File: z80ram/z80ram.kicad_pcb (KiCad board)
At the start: 2 copper layers, 99.8 x 49.9 mm, 19 parts, among them J1 BUS, J2 BUSEXT, Q1 2N7000, U1 Z80CPU, U2 74HCT574, U3 74LS257, U4 AS6C4008-55PCN, U5 74LS138, U6 DS1302+, Y1 XTAL

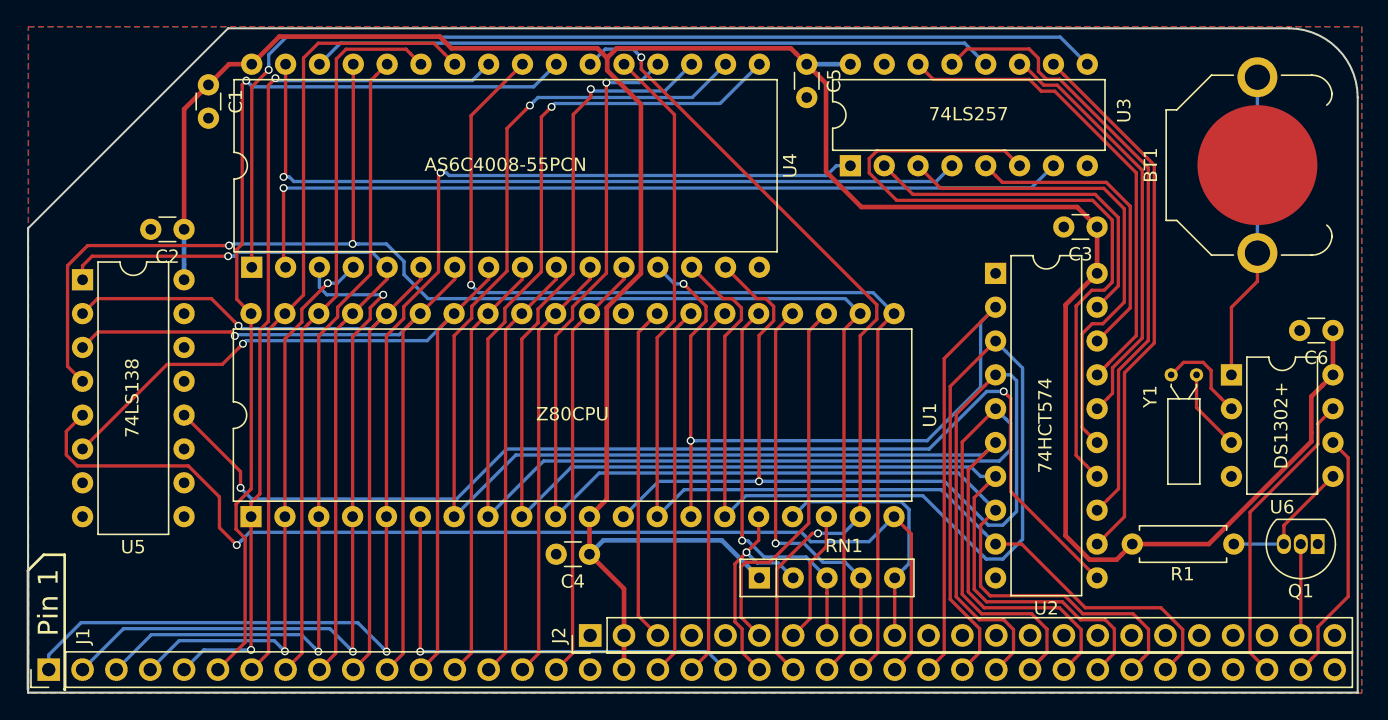
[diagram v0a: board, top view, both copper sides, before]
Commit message: Fix address decoding, minor REV2 tweaks
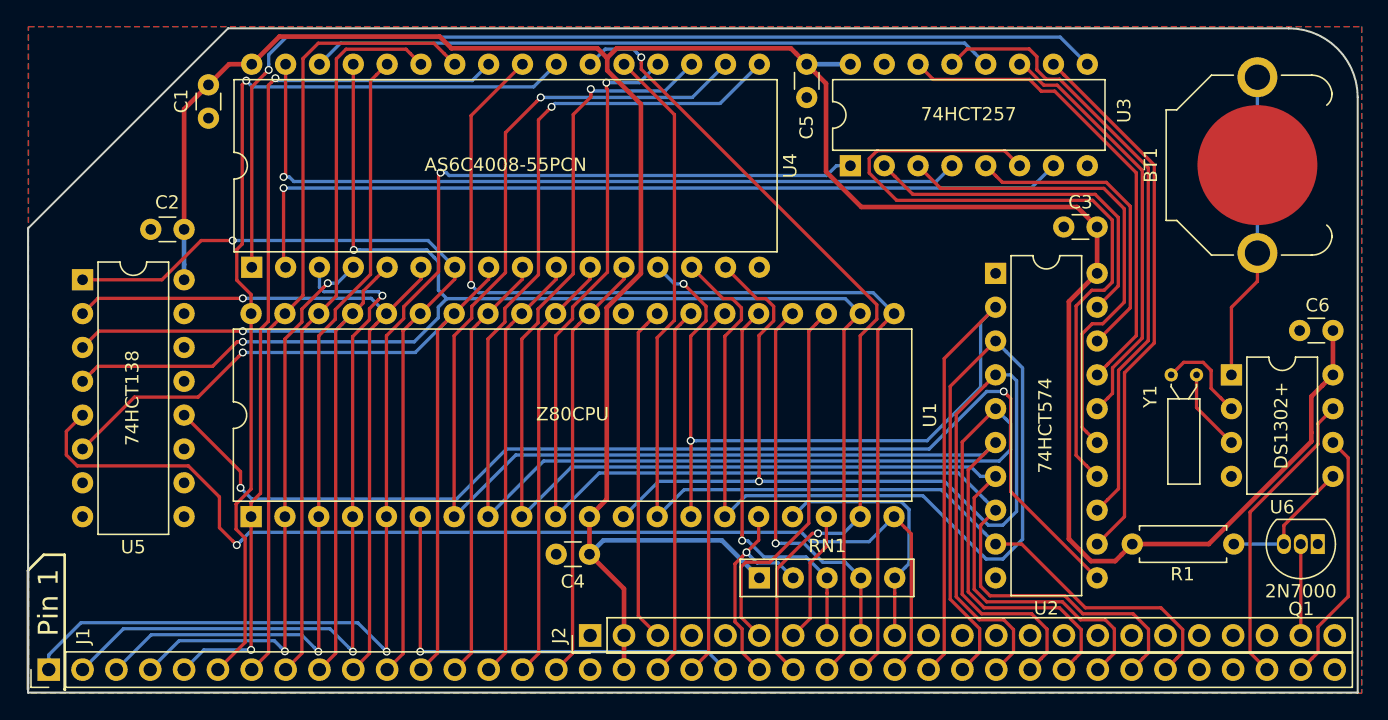
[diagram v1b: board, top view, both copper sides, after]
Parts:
- C1, C2, C3, C4, C5, C6: value C -> 0.1uf
- R1: value R -> 1M
- U3: value 74LS257 -> 74HCT257
- U5: value 74LS138 -> 74HCT138
- Y1: value XTAL -> 32.768kHz
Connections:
- U5 pad 1: /A7 -> /A5
- U5 pad 3: /A5 -> /A7
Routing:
- net /A7: track 57.1 -> 53.6 mm
- net /A5: track 59.0 -> 62.3 mm
- net /A6: track 57.0 -> 56.1 mm
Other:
- board text added: "z80ctrl CPU/RAM/RTC Board REV2 (C)2020 J.B. Langston https://github.com/jblang/z80ctrl"
- board text removed: "z80ctrl CPU/RAM/RTC Board REV1 (C)2020 J.B. Langston https://github.com/jblang/z80ctrl"

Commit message: Fix VCC1/VCC2 mixup on RTC, better layout for RTC crystal
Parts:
- R1: value 1M -> 10K
- moved C6 17.5 mm to (237.9, 136.3), turned to 90 degrees
- moved R1 16.7 mm to (240.8, 126.0)
- moved Y1 9.59 mm to (243.7, 138.3)
- moved U6 7.73 mm to (240.9, 136.3), turned to 90 degrees
- moved Q1 3.44 mm to (248.4, 144.5), turned to 0 degrees
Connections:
- U6 pad 1: Net-(BT1-Pad1) -> VCC
- U6 pad 8: VCC -> Net-(BT1-Pad1)
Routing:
- net Net-(Q1-Pad3): track 10.4 -> 19.6 mm
- net /MISO: track 19.0 -> 26.9 mm
- net VCC: track 217.2 -> 211.7 mm
- net /SCK: track 22.7 -> 27.9 mm
- net Net-(U6-Pad2): track 7.14 -> 2.13 mm
- net Net-(U6-Pad3): track 6.17 -> 2.13 mm
- net /~AUXCS1: track 6.86 -> 4.54 mm
- net Net-(BT1-Pad1): track 23.1 -> 23.9 mm
